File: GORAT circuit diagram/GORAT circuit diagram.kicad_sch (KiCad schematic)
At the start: 73 parts, among them J1 AudioJack2, J10 Conn_01x02_Socket, J11 Conn_01x02_Socket, J2 AudioJack2, J3 Conn_01x08_Socket, J4 Conn_01x08_Socket, J5 Conn_01x02_Socket, J6 Barrel_Jack, J7 Conn_01x02_Socket, J8 Conn_01x02_Socket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

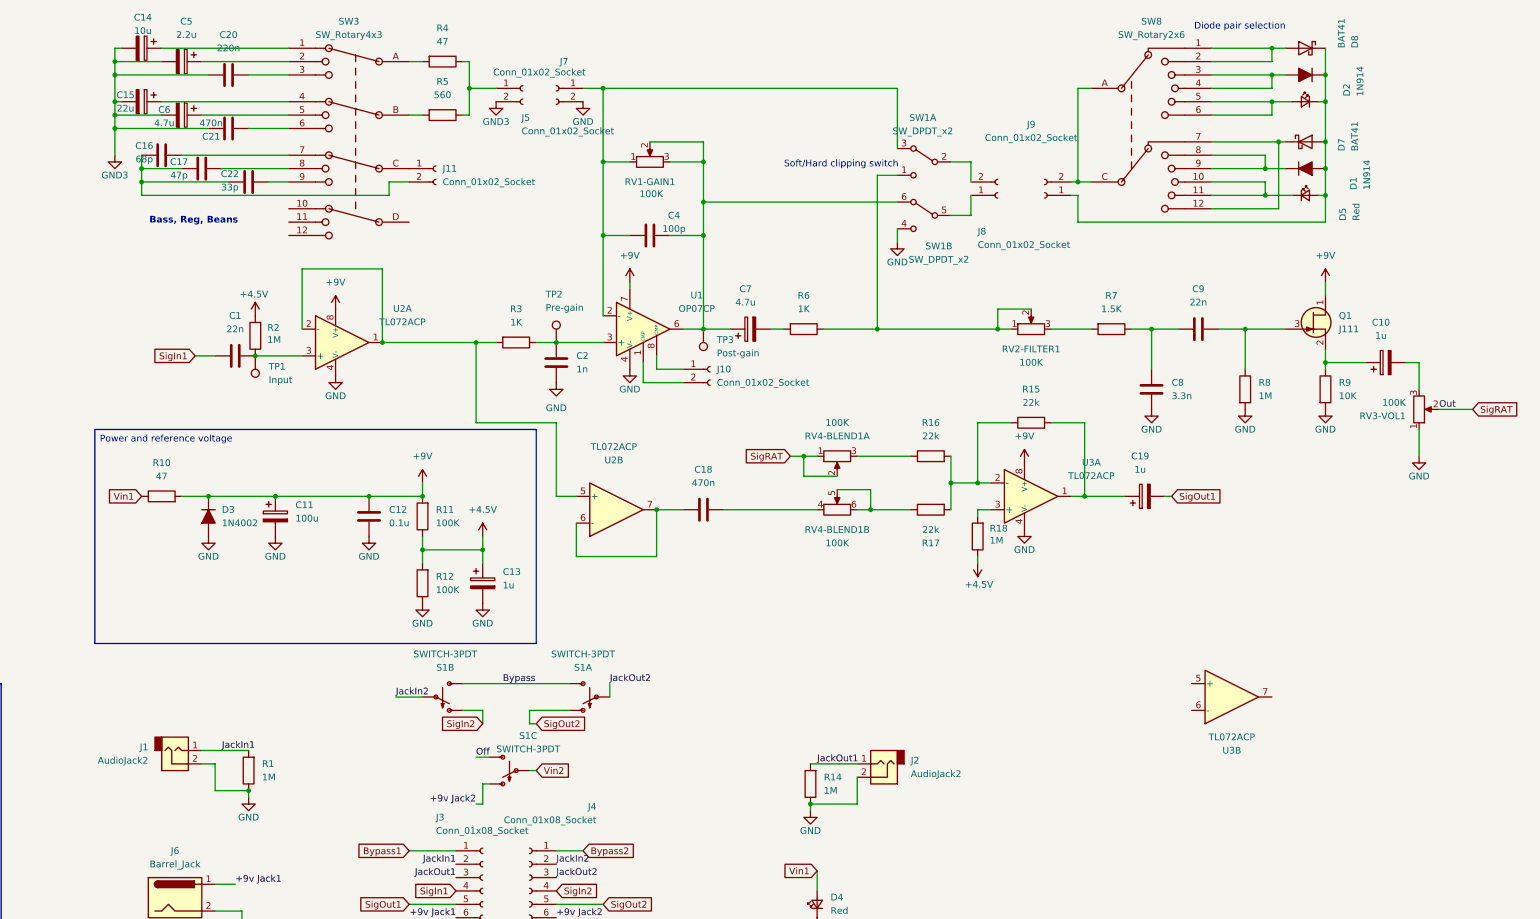
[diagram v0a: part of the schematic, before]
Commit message: Update KiCad schematic and PCB to v1.3
Add new KiCad schematic 'GORAT circuit diagram 1.3.kicad_sch' and v1.3 PCB/project files; modify existing GORAT schematic, PCB (.kicad_pcb) and project library (.kicad_prl). Add multiple backup ZIP archives, remove an autosave temp file, and update Build_Guide.docx. Prepares project files for the v1.3 schematic/PCB update and cleans up temporary autosave artifacts.
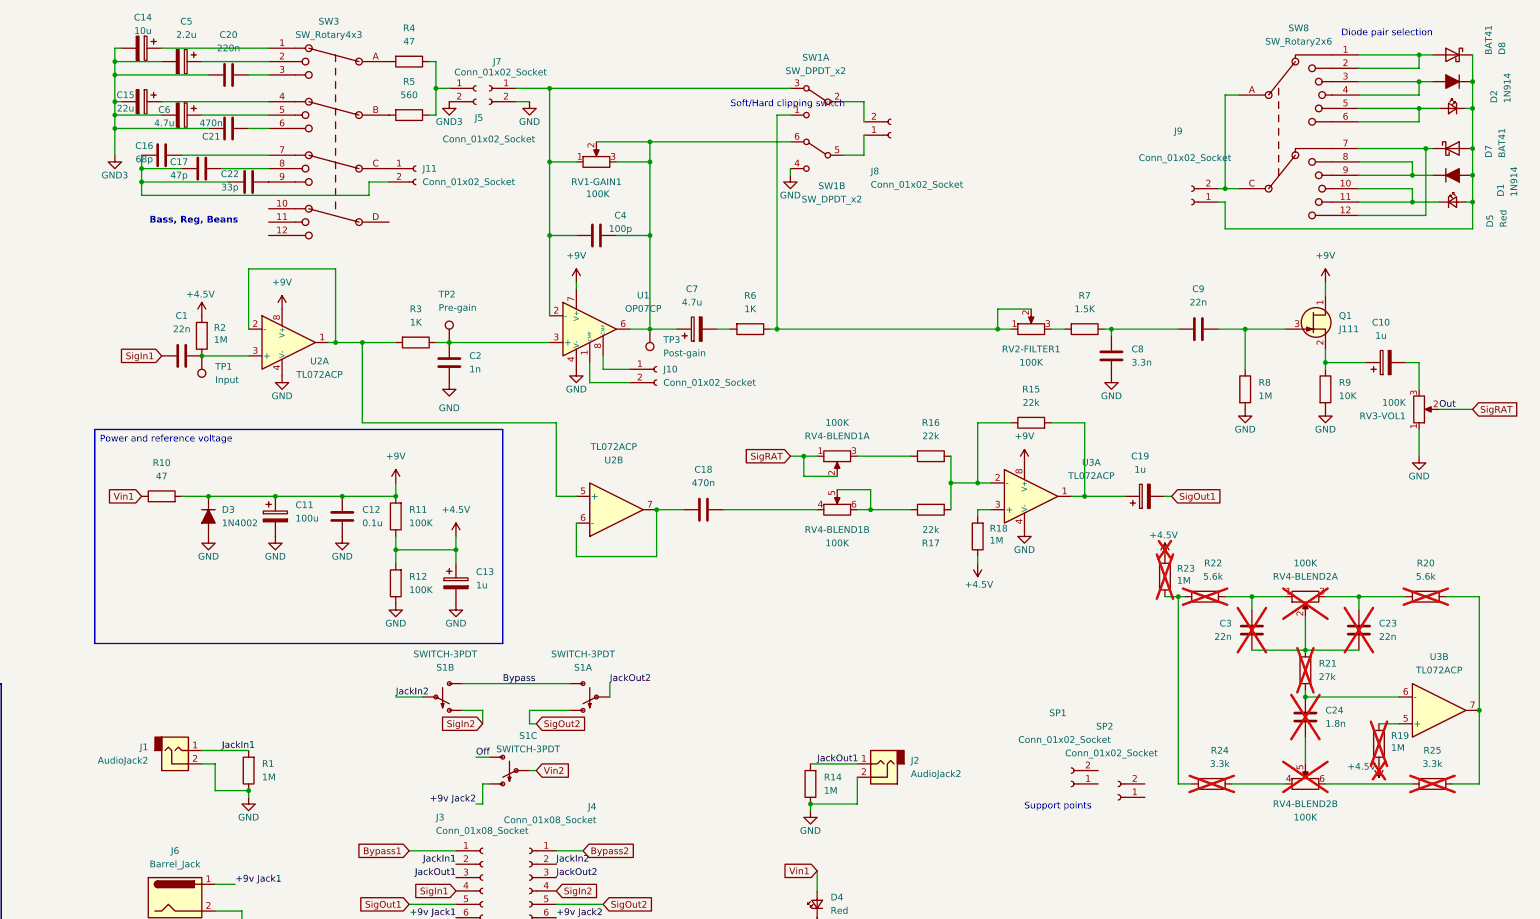
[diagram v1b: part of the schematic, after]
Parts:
- added C23, C3: 22n, Capacitor_THT:C_Disc_D4.7mm_W2.5mm_P5.00mm, symbol Device:C
- added C24: 1.8n, Capacitor_THT:C_Disc_D4.7mm_W2.5mm_P5.00mm, symbol Device:C
- added R19, R23: 1M, Resistor_THT:R_Axial_DIN0207_L6.3mm_D2.5mm_P10.16mm_Horizontal, symbol Device:R
- added R20, R22: 5.6k, Resistor_THT:R_Axial_DIN0207_L6.3mm_D2.5mm_P10.16mm_Horizontal, symbol Device:R
- added R21: 27k, Resistor_THT:R_Axial_DIN0207_L6.3mm_D2.5mm_P10.16mm_Horizontal, symbol Device:R
- added R24, R25: 3.3k, Resistor_THT:R_Axial_DIN0207_L6.3mm_D2.5mm_P10.16mm_Horizontal, symbol Device:R
- added RV4-BLEND2: 100K, Potentiometer_THT:Potentiometer_Alpha_RD902F-40-00D_Dual_Vertical, symbol Device:R_Potentiometer_Dual_Separate
- added SP1, SP2: Conn_01x02_Socket, Connector_PinHeader_2.54mm:PinHeader_1x02_P2.54mm_Vertical, symbol Connector:Conn_01x02_Socket
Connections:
- net +4.5V: now also R19.1, R23.2
- net at U3.5 (+): now also R19.2
- net at U3.6 (-): now also C24.2, R21.1
- net at U3.7: now also R20.2, R25.2
- new net: C23.1, C3.1, R21.2, RV4-BLEND2.2
- new net: C3.2, R22.2, RV4-BLEND2.1
- new net: C23.2, R20.1, RV4-BLEND2.3
- new net: R22.1, R23.1, R24.1
- new net: R24.2, RV4-BLEND2.4
- new net: C24.1, RV4-BLEND2.5
- new net: R25.1, RV4-BLEND2.6
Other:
- note added: "Support points"
- moved on the sheet: C1, C12, C13, C2, C4, C7, C8, D1, D2, D5, D7, D8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

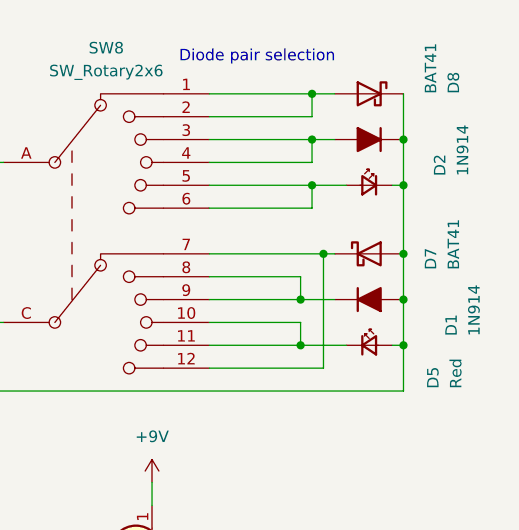
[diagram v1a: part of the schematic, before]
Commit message: Adjust KiCad schematic junctions and wires
Rearranged junctions and wires in GORAT circuit diagram.kicad_sch to correct routing and updated related UUIDs; also moved several diode symbol positions (D1, D2, D7, D8). Added two new schematic backup ZIPs (2026-04-06) and removed an older backup (2026-03-20). Deleted temporary .lck lock files generated by KiCad.
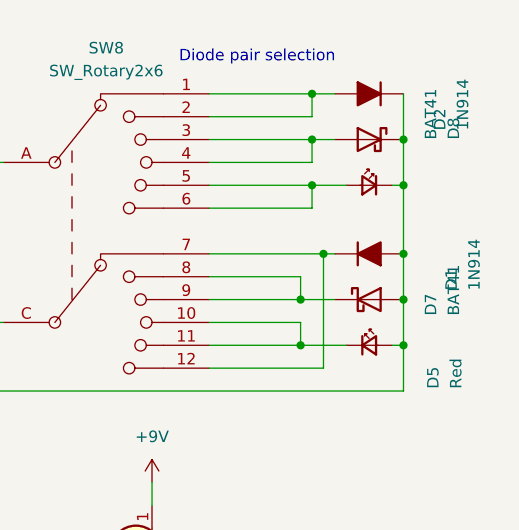
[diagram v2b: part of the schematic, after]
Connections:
- net at SW8.1, SW8.2: now also D2.2 (A); no longer D8.2 (A)
- net at SW8.3, SW8.4: now also D8.2 (A); no longer D2.2 (A)
- net at SW8.12, SW8.7: now also D1.1 (K); no longer D7.1 (K)
- net at SW8.8, SW8.9: now also D7.1 (K); no longer D1.1 (K)
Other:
- moved on the sheet: D1, D2, D7, D8

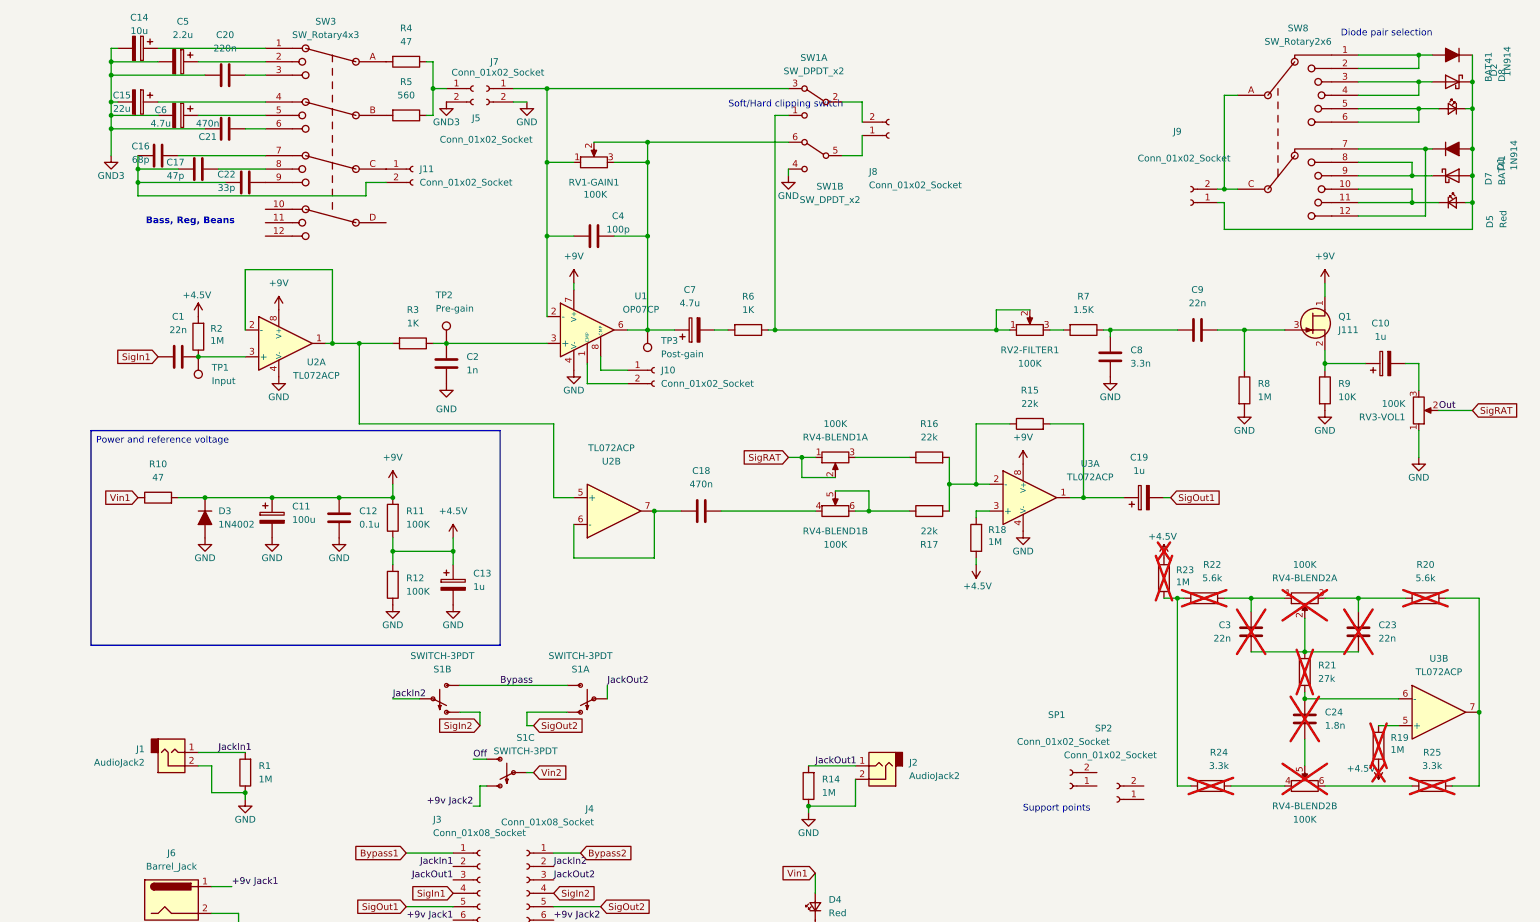
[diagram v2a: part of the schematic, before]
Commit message: Update Build_Guide and add GORAT backup zip
Update Build_Guide.docx (documentation changes) and add a new backup ZIP for the GORAT circuit diagram: GORAT circuit diagram-2026-04-04_053106.zip under the backups folder.
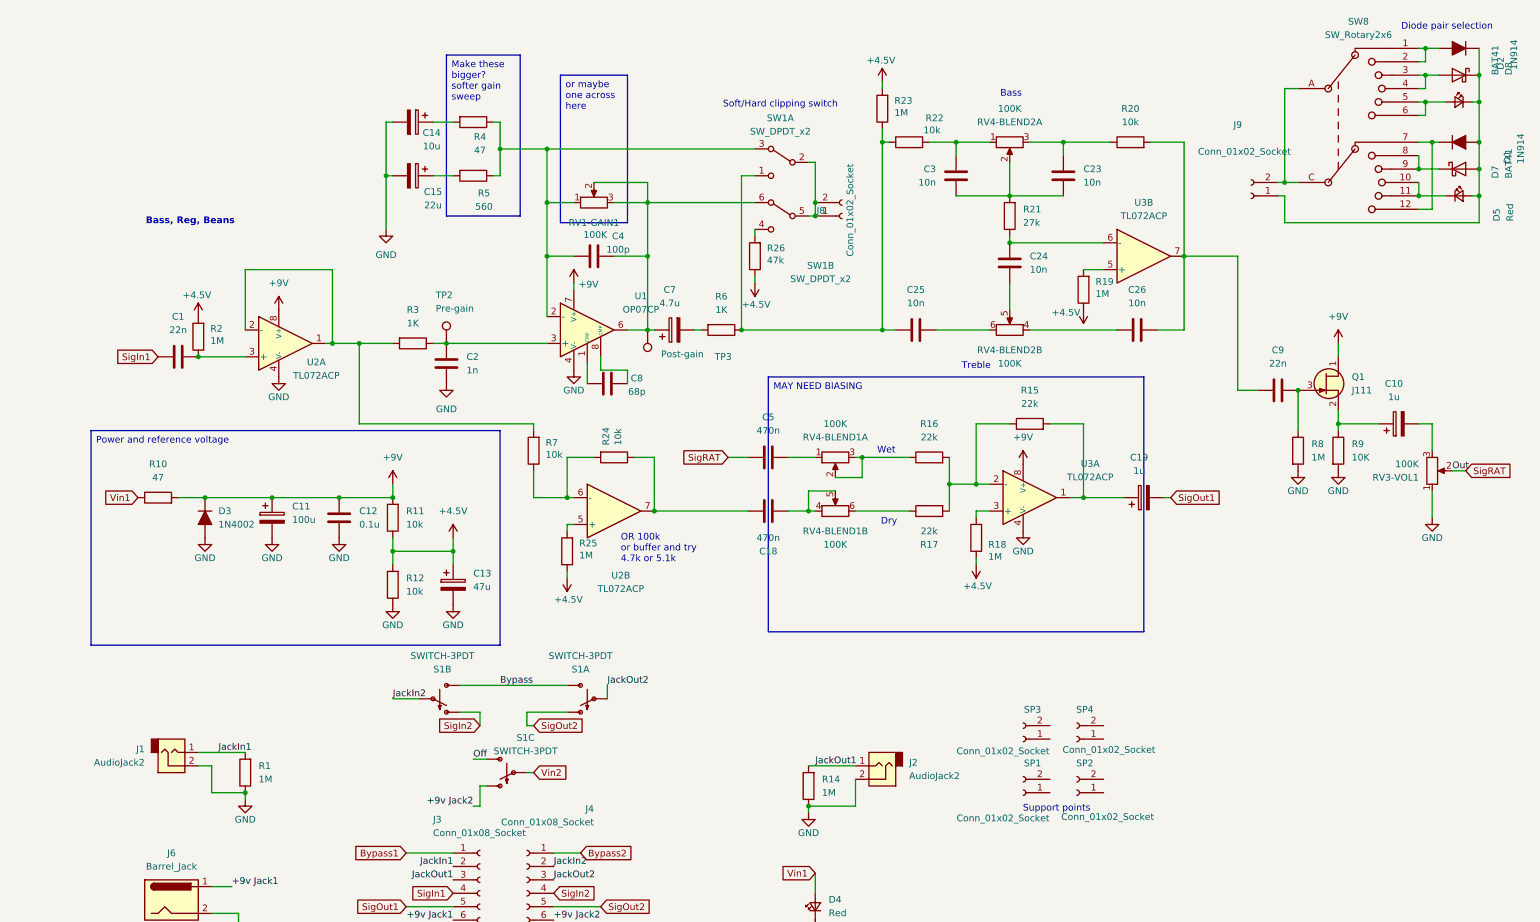
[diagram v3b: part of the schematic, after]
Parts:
- removed C16: 68p, Capacitor_THT:C_Disc_D4.7mm_W2.5mm_P5.00mm, symbol Device:C
- removed C17: 47p, Capacitor_THT:C_Disc_D4.7mm_W2.5mm_P5.00mm, symbol Device:C
- removed C20: 220n, Capacitor_THT:C_Disc_D4.7mm_W2.5mm_P5.00mm, symbol Device:C
- removed C21: 470n, Capacitor_THT:C_Disc_D4.7mm_W2.5mm_P5.00mm, symbol Device:C
- removed C22: 33p, Capacitor_THT:C_Disc_D4.7mm_W2.5mm_P5.00mm, symbol Device:C
- removed C5: 2.2u, Capacitor_THT:CP_Radial_D5.0mm_P2.50mm, symbol Device:C_Polarized
- removed C6: 4.7u, Capacitor_THT:CP_Radial_D5.0mm_P2.50mm, symbol Device:C_Polarized
- removed J10, J11, J5, J7: Conn_01x02_Socket, Connector_PinHeader_2.54mm:PinHeader_1x02_P2.54mm_Vertical, symbol Connector:Conn_01x02_Socket
- removed RV2-FILTER1: 100K, Daves customs:Potentiometer_Alpha_RD901F-40-00D_Single_Vertical, symbol Device:R_Potentiometer
- removed SW3: SW_Rotary4x3, Daves customs:RS26, symbol KRS_Switch:SW_Rotary4x3
- removed TP1: Input, TestPoint:TestPoint_Pad_D2.0mm, symbol Connector:TestPoint
- added C25, C26: 10n, Capacitor_THT:C_Disc_D4.7mm_W2.5mm_P5.00mm, symbol Device:C
- added C5: 470n, Capacitor_THT:C_Disc_D4.7mm_W2.5mm_P5.00mm, symbol Device:C
- added R26: 47k, Resistor_THT:R_Axial_DIN0207_L6.3mm_D2.5mm_P10.16mm_Horizontal, symbol Device:R
- added SP3, SP4: Conn_01x02_Socket, Connector_PinHeader_2.54mm:PinHeader_1x02_P2.54mm_Vertical, symbol Connector:Conn_01x02_Socket
- C13: value 1u -> 47u
- C23, C3: value 22n -> 10n; now fitted; now in the parts list
- C24: value 1.8n -> 10n; now fitted; now in the parts list
- C8: value 3.3n -> 68p
- R11, R12: value 100K -> 10k
- R19, R21, R23, RV4-BLEND2: now fitted; now in the parts list
- R20, R22: value 5.6k -> 10k; now fitted; now in the parts list
- R24: value 3.3k -> 10k; now fitted; now in the parts list
- R25: value 3.3k -> 1M; now fitted; now in the parts list
- R7: value 1.5K -> 10k
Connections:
- net GND3 is gone; now on net GND: C14.2, C15.2
- net +4.5V: now also R25.1, R26.1
- net GND: no longer C8.1, SW1.4 (A)
- net SigRAT: now also C5.1; no longer RV4-BLEND1.1, RV4-BLEND1.2
- net at C4.2, RV1-GAIN1.1, SW1.3 (C)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: now also R4.1, R5.1
- net at R5.2: now also C15.1
- net at J8.1 (Pin_1), SW1.5 (B): now also J8.2 (Pin_2), SW1.2 (B)
- net at R17.1, RV4-BLEND1.6: no longer RV4-BLEND1.5
- net at R6.1, SW1.1 (A): now also R22.1, R23.1, C25.2
- net at U1.1 (CMP): now also C8.1
- net at U1.8 (CMP): now also C8.2
- net at R4.2: now also C14.1
- net at R3.2, U2.1, U2.2 (-): now also R7.2; no longer U2.5 (+)
- net at C18.1, U2.7: now also R24.1; no longer U2.6 (-)
- net at R24.2: now also R7.1, U2.6 (-); no longer RV4-BLEND2.4
- net at R16.1, RV4-BLEND1.3: now also RV4-BLEND1.2
- net at R20.2, U3.7: now also C9.2, C26.1; no longer R25.2
- net at RV4-BLEND2.6: now also C25.1; no longer R25.1
- net at C18.2, RV4-BLEND1.4: now also RV4-BLEND1.5
- new net: C5.2, RV4-BLEND1.1
- new net: C26.2, RV4-BLEND2.4
- new net: R26.2, SW1.4 (A)
- new net: R25.2, U2.5 (+)
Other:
- note added: "Bass"
- note added: "Dry"
- note added: "OR 100k or buffer and try 4.7k or 5.1k"
- note added: "Treble"
- note added: "Wet"
- moved on the sheet: C10, C14, C15, C18, C4, C7, C9, D1, D2, D5, D7, D8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

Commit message: potentially fixed volume mixer
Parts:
- removed C10: 1u, Capacitor_THT:CP_Radial_D5.0mm_P2.50mm, symbol Device:C_Polarized
- removed RV4-BLEND1: 100K, Potentiometer_THT:Potentiometer_Alpha_RD902F-40-00D_Dual_Vertical, symbol Device:R_Potentiometer_Dual_Separate
- added RV4-VOLDry1: 100K, Daves customs:Potentiometer_Alpha_RD901F-40-00D_Single_Vertical, symbol Device:R_Potentiometer
- C18, C5: value 470n -> 1u
- R15: value 22k -> 100k
- R18: value 1M -> 22k
- renumbered RV3-VOL1 to RV3-VOLWet1
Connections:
- net GND: now also RV4-VOLDry1.1
- net SigRAT: now also Q1.2 (S), R9.1; no longer RV3-VOLWet1.2
- net at RV3-VOLWet1.3: now also C5.2
- net at R17.1: now also RV4-VOLDry1.2
- net at R16.2, R17.2: now also U3.3 (+); no longer R15.1, U3.2 (-)
- net at R16.1: now also RV3-VOLWet1.2
- net at R18.2: now also R15.1, U3.2 (-); no longer U3.3 (+)
- net at C18.2: now also RV4-VOLDry1.3
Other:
- moved on the sheet: C5, R15, R17, RV3-VOLWet1

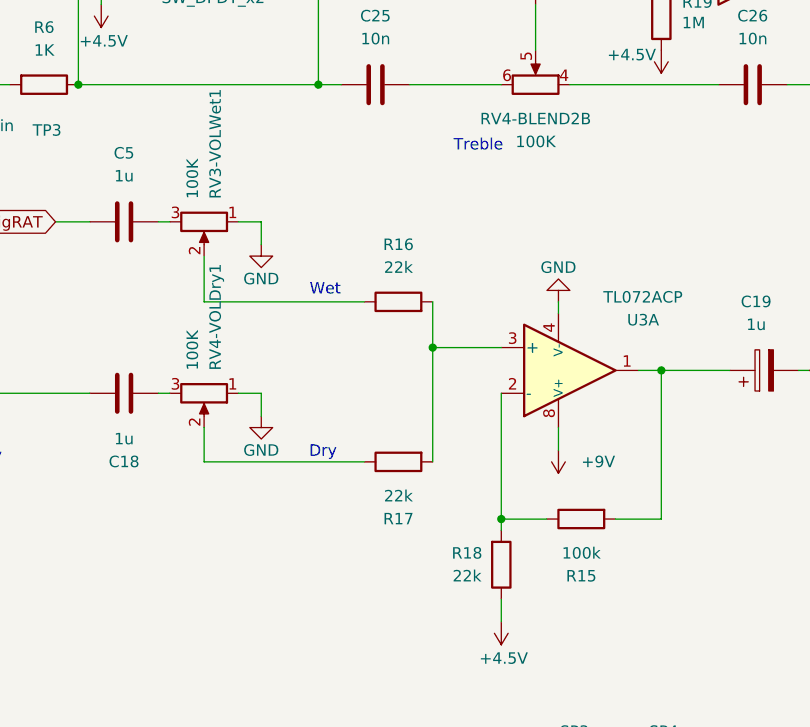
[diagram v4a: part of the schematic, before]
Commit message: Schematic: add +5V, C6, R27; adjust wires
Added a +5V power symbol, C6 (1u) and R27 (47k); adjusted component positions, junctions and wire routing to match the new connections. Updated a resistor value from 100k to 10k and corrected several UUIDs for wires/junctions. Also updated autosave path and KiCad .lck metadata and renamed a few backup zip files. These changes update schematic connectivity and component placement.
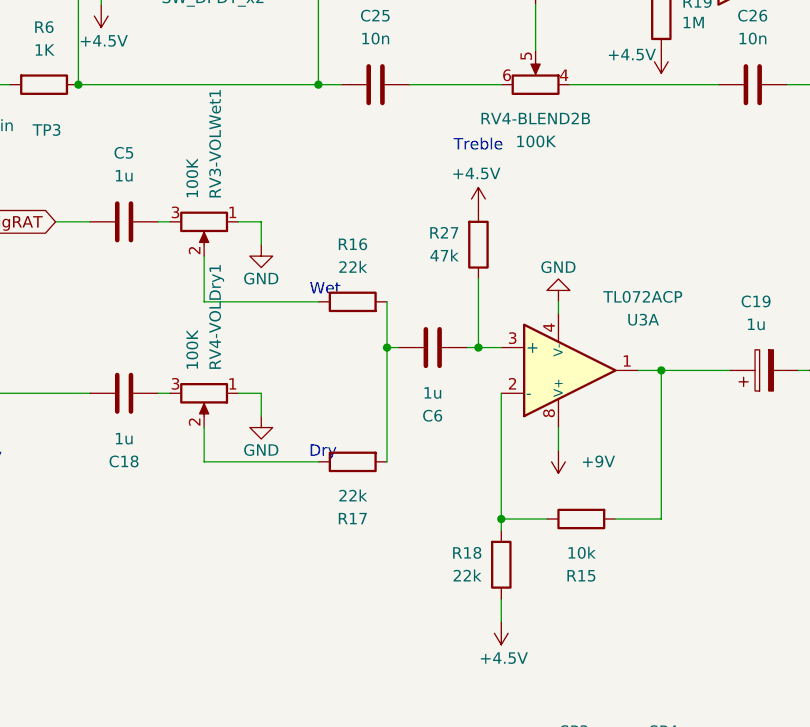
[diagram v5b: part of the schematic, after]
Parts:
- added C6: 1u, Capacitor_THT:C_Disc_D4.7mm_W2.5mm_P5.00mm, symbol Device:C
- added R27: 47k, Resistor_THT:R_Axial_DIN0207_L6.3mm_D2.5mm_P10.16mm_Horizontal, symbol Device:R
- R15: value 100k -> 10k
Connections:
- net +4.5V: now also R27.2
- net at R16.2, R17.2: now also C6.1; no longer U3.3 (+)
- new net: C6.2, R27.1, U3.3 (+)
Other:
- moved on the sheet: R16, R17
